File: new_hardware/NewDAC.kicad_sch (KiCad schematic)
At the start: 63 parts, among them J1 PJ-322, U1 PCM1795, U14 OPA1656, U15 OPA1656, U6 LM4562, U7 LM4562

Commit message: some changes
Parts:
- C104, C105, C108, C109, C80, C81, C84, C85, C86, C87, C88, C89, C90, C91: Mnfct.  partnumber T491A106K010AT -> (none)
- R48, R49, R50, R51, R52, R53, R54, R55, R56, R57, R58, R59, R60, R61, R62, R63, R64, R65, R66, R67: footprint (none) -> rlib_passive:R_0603_1608Metric

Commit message: xxxx
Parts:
- C28: renamed from C79; footprint (none) -> rlib_passive:C_0603_1608Metric
- C32: renamed from C85; value 10u -> 100n; footprint rlib_passive:T491A106K010AT -> rlib_passive:R_0603_1608Metric
- C33: renamed from C86; value 10u -> 100n; footprint rlib_passive:T491A106K010AT -> rlib_passive:R_0603_1608Metric
- C41: renamed from C94; footprint (none) -> rlib_passive:C_0603_1608Metric
- C42: renamed from C96; footprint (none) -> rlib_passive:C_0603_1608Metric
- C43: renamed from C97; footprint (none) -> rlib_passive:C_0603_1608Metric
- C44: renamed from C95; footprint (none) -> rlib_passive:C_0603_1608Metric
- C47: renamed from C98; footprint (none) -> rlib_passive:C_0603_1608Metric
- C48: renamed from C99; footprint (none) -> rlib_passive:C_0603_1608Metric
- C49: renamed from C100; footprint (none) -> rlib_passive:C_0603_1608Metric
- C50: renamed from C101; footprint (none) -> rlib_passive:C_0603_1608Metric
- C51: renamed from C102; footprint (none) -> rlib_passive:C_0603_1608Metric
- C52: renamed from C103; footprint (none) -> rlib_passive:C_0603_1608Metric
- TP13: renamed from TP20; footprint (none) -> TestPoint:TestPoint_Pad_D1.0mm
- TP14: renamed from TP21; footprint (none) -> TestPoint:TestPoint_Pad_D1.0mm
- renumbered C80 to C29, C81 to C30, C84 to C31, C82 to C34, C83 to C35, C87 to C36, C88 to C37, C89 to C38, C90 to C39, C91 to C40, C92 to C45, C93 to C46, C104 to C53, C105 to C54, C106 to C55, C107 to C56, C108 to C57, C109 to C58, C110 to C59, C111 to C60, D12 to D10, D11 to D9, J1 to J2, R48 to R23, R50 to R24, R51 to R25, R53 to R26, R54 to R27, R52 to R28, R56 to R29, R57 to R30, R49 to R31, R55 to R32, R58 to R33, R59 to R34, R60 to R35, R61 to R36, R62 to R37, R63 to R38, R64 to R39, R65 to R40, R66 to R41, R67 to R42, U1 to U4, U6 to U5, U7 to U6, U14 to U7, U15 to U8

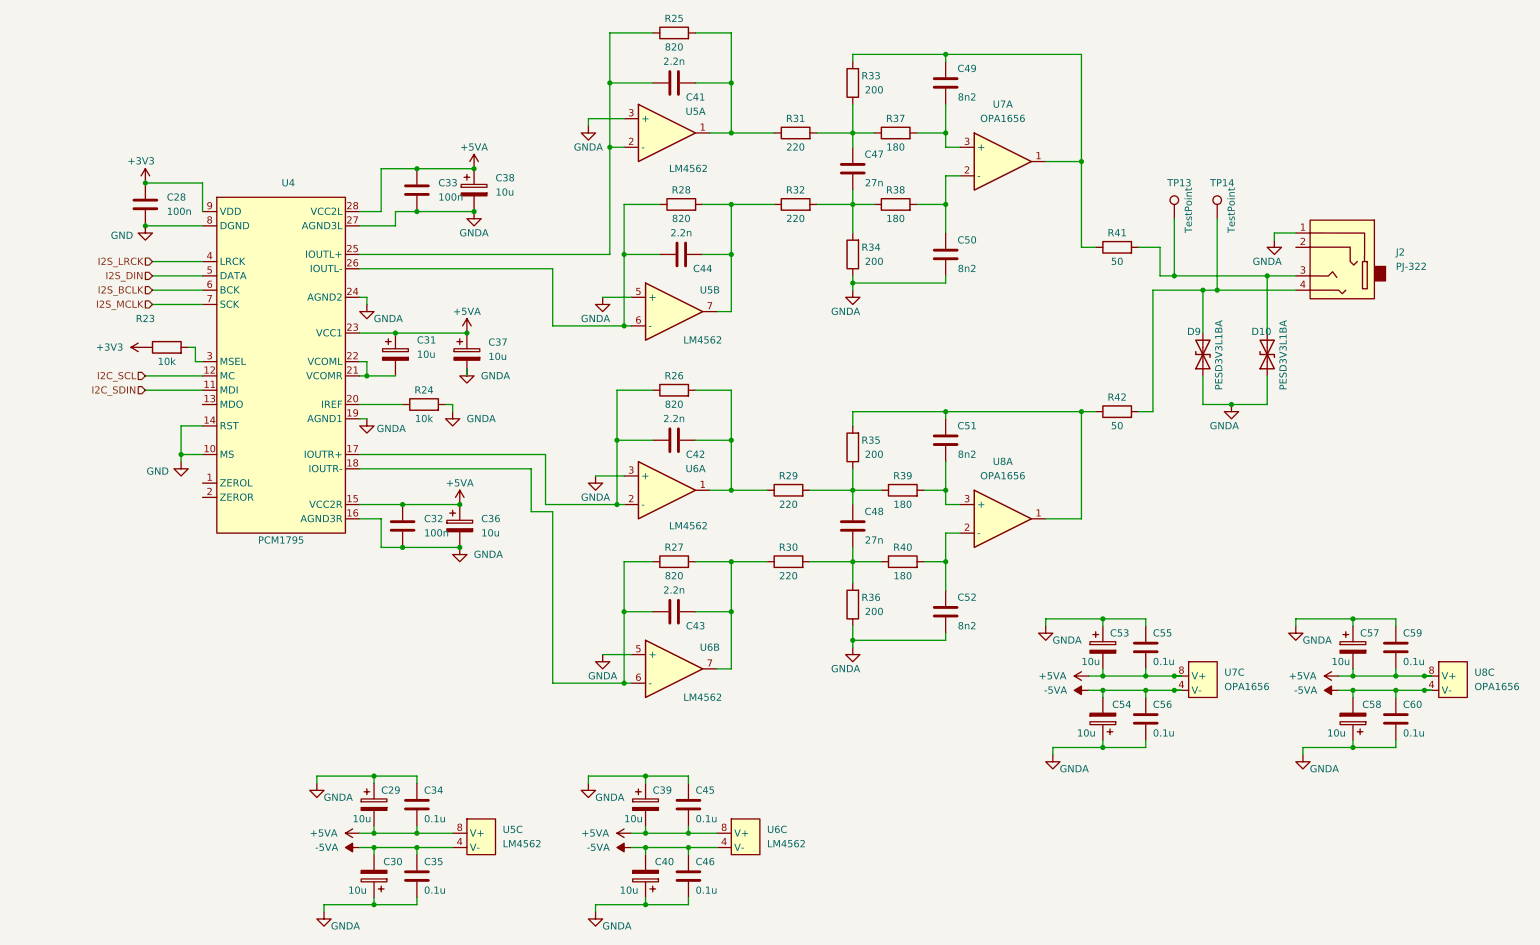
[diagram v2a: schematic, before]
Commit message: changed lcd interface and layout is partly made
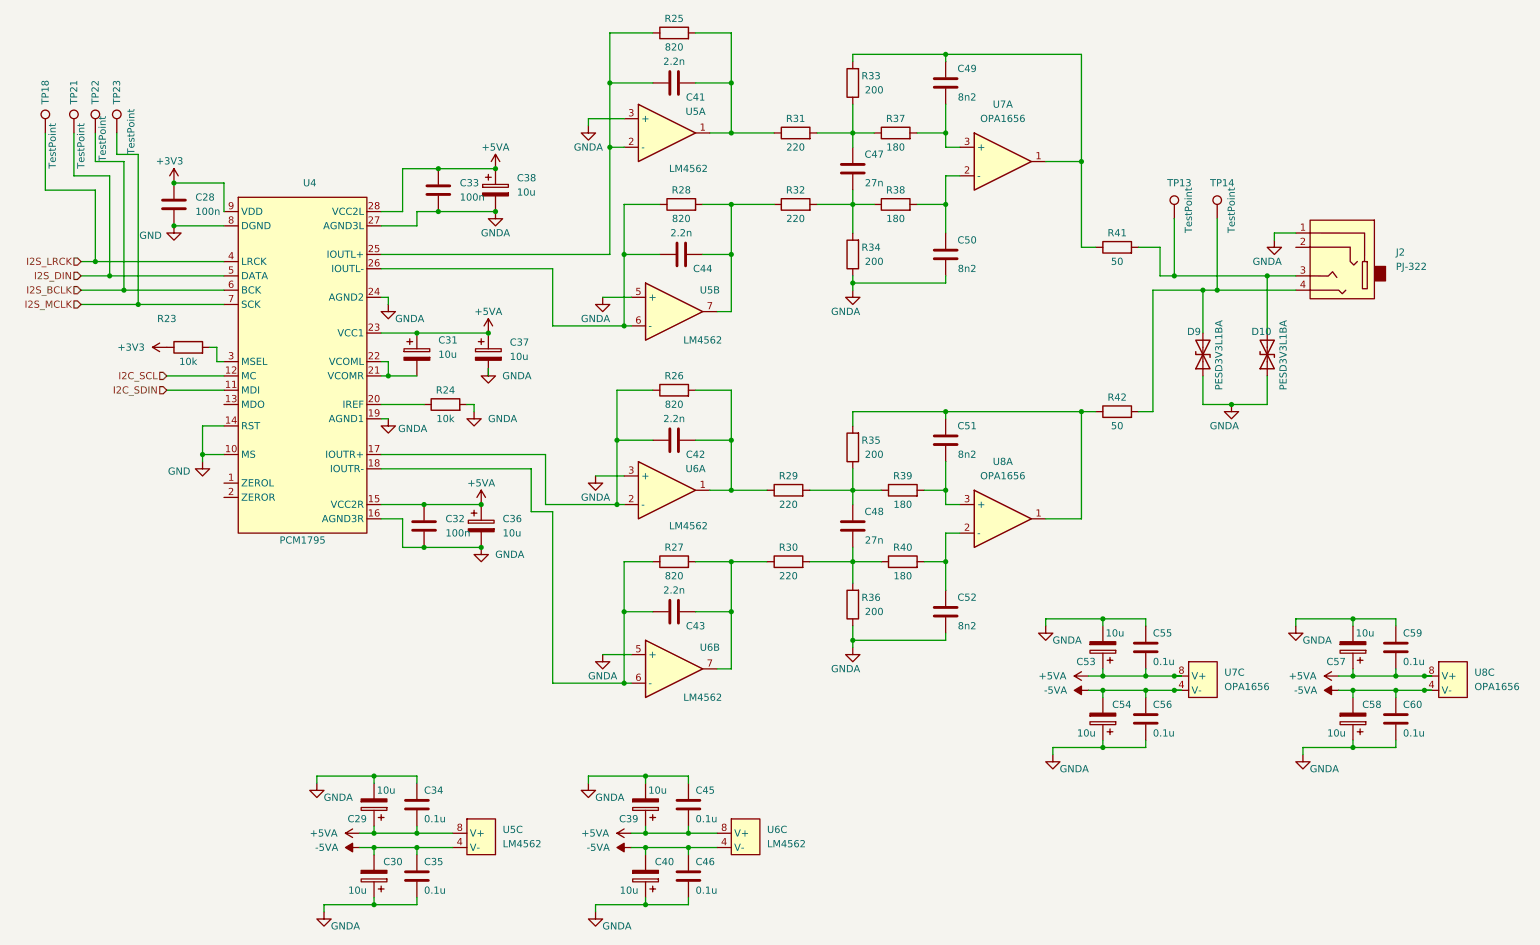
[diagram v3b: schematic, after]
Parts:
- added TP18, TP21, TP22, TP23: TestPoint, TestPoint:TestPoint_Pad_D1.0mm, symbol Connector:TestPoint
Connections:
- net +5VA: now also C29.1, C39.1, C53.1, C57.1; no longer C29.2, C39.2, C53.2, C57.2
- net GNDA: now also C29.2, C39.2, C53.2, C57.2; no longer C29.1, C39.1, C53.1, C57.1
- net I2S_BCLK: now also TP22.1
- net I2S_DIN: now also TP21.1
- net I2S_LRCK: now also TP18.1
- net I2S_MCLK: now also TP23.1
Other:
- moved on the sheet: C28, C29, C31, C32, C33, C36, C37, C38, C39, C53, C57, R23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

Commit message: some fucking changes
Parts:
- removed C56, C59, C60: 0.1u, rlib_passive:C_0603_1608Metric, symbol rlib_passive:C
- added C16, C20, C7: 100n, rlib_passive:C_0603_1608Metric, symbol rlib_passive:C
- C28: LCSC partnumber (none) -> C45000; Manufacturer (none) -> Murata; Mnfct. partnumber (none) -> GRM188R71C104KA01D
- C29, C30, C31, C36, C37, C38, C39, C40, C54, C57, C58: LCSC partnumber (none) -> C1508940; Manufacturer (none) -> Kemet; Mnfct. partnumber (none) -> T491A106K010AT
- C32, C33: footprint rlib_passive:R_0603_1608Metric -> rlib_passive:C_0603_1608Metric; LCSC partnumber (none) -> C45000; Manufacturer (none) -> Murata; Mnfct. partnumber (none) -> GRM188R71C104KA01D
- C34, C35, C45, C46, C55: value 0.1u -> 100n; LCSC partnumber (none) -> C45000; Manufacturer (none) -> Murata; Mnfct. partnumber (none) -> GRM188R71C104KA01D
- C41, C42, C43, C44: LCSC partnumber (none) -> C882523; Manufacturer (none) -> YAGEO; Mnfct. partnumber (none) -> GRM1885C1H222FA01D
- C47, C48: LCSC partnumber (none) -> C107086; Manufacturer (none) -> YAGEO; Mnfct. partnumber (none) -> CC0603KRX7R9BB273
- C53: LCSC partnumber (none) -> C1508940; Manufacturer (none) -> Kemet
- D10, D9: LCSC partnumber (none) -> C2827682; Manufacturer (none) -> TECH PUBLIC; Mnfct. partnumber (none) -> PESD3V3L1BA
- R23, R24: LCSC partnumber (none) -> C217687; Manufacturer (none) -> Viking Tech; Mnfct. partnumber (none) -> ARG03FTC1002; Tolerance (none) -> 1%
- R25, R26, R27, R28: LCSC partnumber (none) -> C218157; Manufacturer (none) -> Viking Tech; Mnfct. partnumber (none) -> ARG03FTC8200; Tolerance (none) -> 1%
- R29, R30, R31, R32: LCSC partnumber (none) -> C234383; Manufacturer (none) -> Viking Tech; Mnfct. partnumber (none) -> AR03FTC2200; Tolerance (none) -> 1%
- R33, R34, R35, R36: LCSC partnumber (none) -> C217868; Manufacturer (none) -> Viking Tech; Mnfct. partnumber (none) -> ARG03FTC2000; Tolerance (none) -> 1%
- R37, R38, R39, R40: LCSC partnumber (none) -> C217827; Manufacturer (none) -> Viking Tech; Mnfct. partnumber (none) -> ARG03FTC1800; Tolerance (none) -> 1%
- R41, R42: value 50 -> 51; LCSC partnumber (none) -> C218064; Manufacturer (none) -> Viking Tech; Mnfct. partnumber (none) -> ARG03FTC0510; Tolerance (none) -> 1%
- TP13, TP14, TP18, TP21, TP22, TP23: now left out of the parts list
- U5, U6: LCSC partnumber (none) -> C57367; LSCS partnumber C57367 -> (none)
- U7, U8: LCSC partnumber (none) -> OPA1656IDR; Manufacturer (none) -> Texas Instruments; Mnfct. partnumber (none) -> OPA1656IDR
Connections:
- net +5VA: now also C35.2, C46.2, C20.2, C7.2; no longer C34.2, C45.2, C55.2
- net -5VA: now also C34.1, C45.1, C55.1, C16.1; no longer C35.1, C46.1
- net GNDA: now also C34.2, C35.1, C45.2, C46.1, C55.2, C16.2, C20.1, C7.1; no longer C34.1, C35.2, C45.1, C46.2, C55.1
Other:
- moved on the sheet: C38, C40
